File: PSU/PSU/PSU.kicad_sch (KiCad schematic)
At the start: 22 parts, among them J1 12V AC, J2 Switch, J3 Conn_02x08_Odd_Even, J4 Conn_02x08_Odd_Even, U1 LM7812, U2 LM7912, U3 LM7805_TO220

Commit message: .
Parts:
- removed J4: Conn_02x08_Odd_Even, symbol Connector_Generic:Conn_02x08_Odd_Even
- added J4: Power out, symbol Connector:Screw_Terminal_01x04
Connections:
- net +12V: now also J4.3 (Pin_3)
- net +5V: now also J4.4 (Pin_4)
- net -12V: now also J4.1 (Pin_1)
- net GNDREF: now also J4.2 (Pin_2)
- net CV: no longer names the net of J3.13 (Pin_13)
- net CV: no longer J3.14 (Pin_14)
- net GATE: no longer names the net of J3.15 (Pin_15)
- net GATE: no longer J3.16 (Pin_16)
- no-connect marks 0 -> 4
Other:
- moved on the sheet: C10

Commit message: .
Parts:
- added C11: 1uF, symbol Device:C_Small
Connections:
- net +12V: now also C11.1
- net GNDREF: now also C11.2
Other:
- moved on the sheet: C10, C7, C8, C9, D3, U1, U2

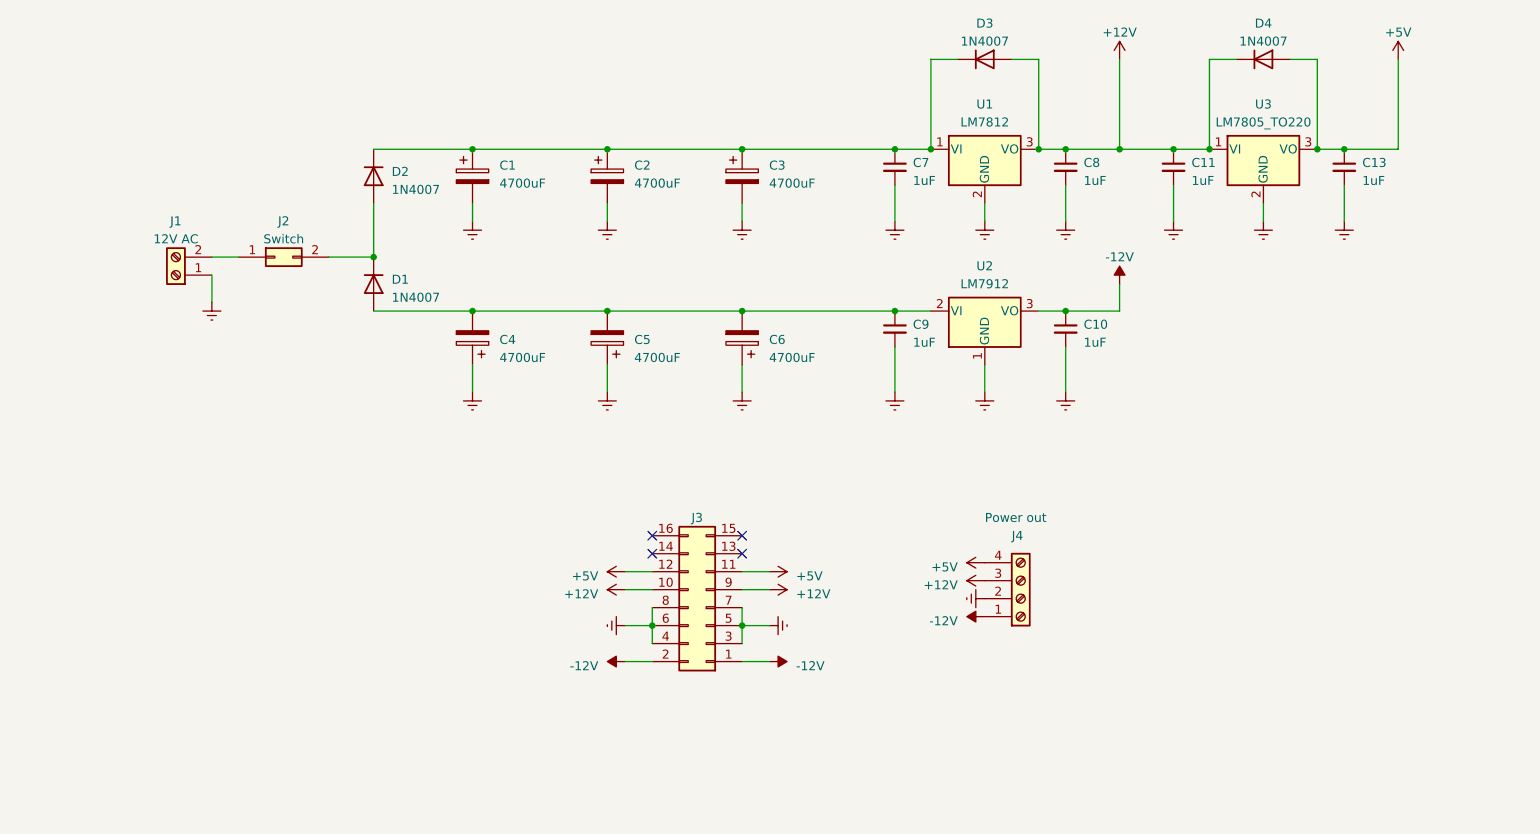
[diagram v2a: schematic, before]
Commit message: Option for center tapped transformer
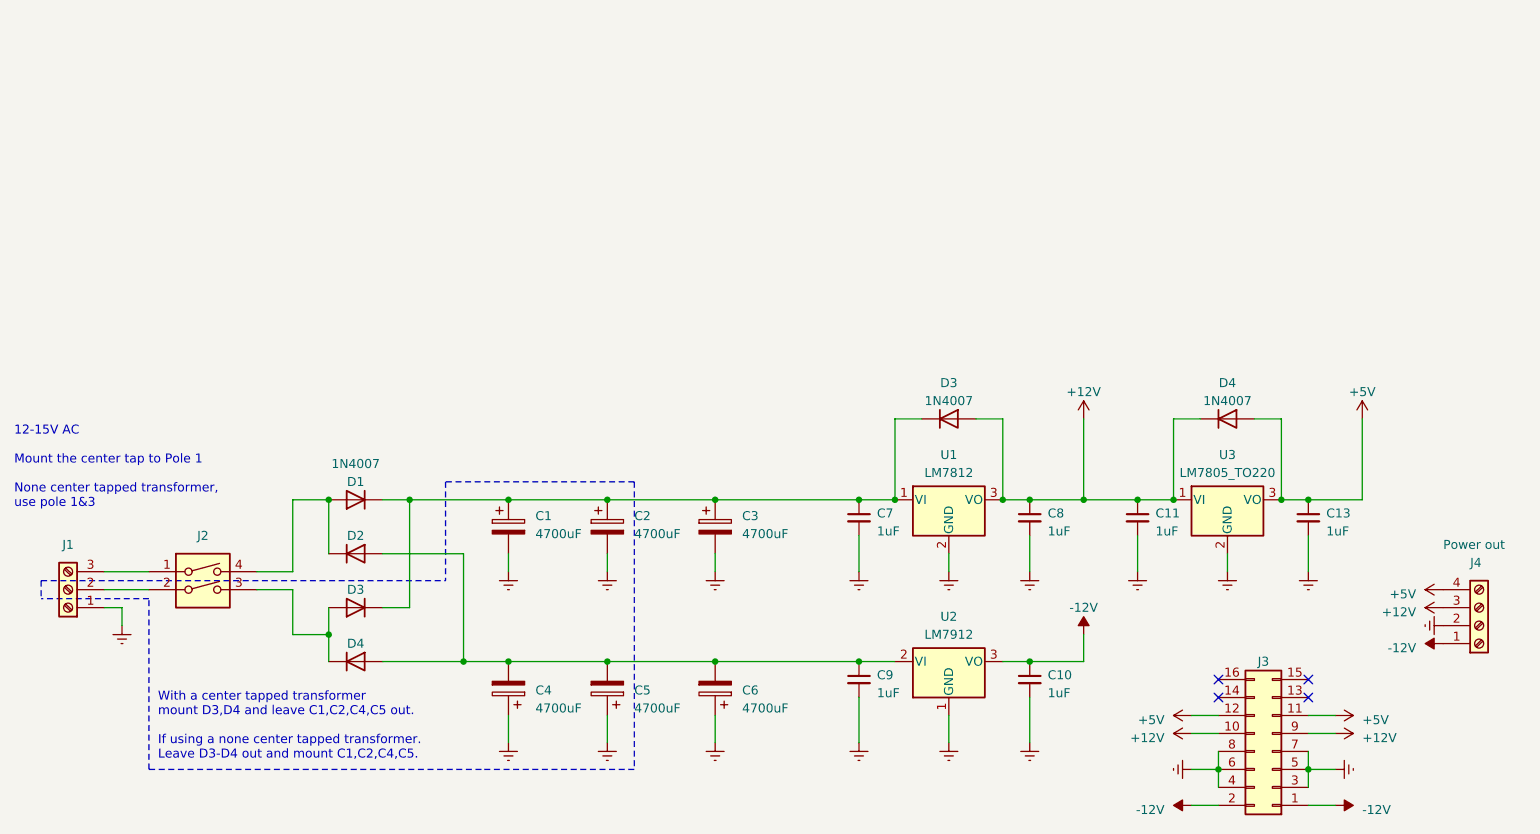
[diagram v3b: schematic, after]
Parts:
- removed J1: 12V AC, symbol Connector:Screw_Terminal_01x02
- removed J2: Switch, symbol Connector_Generic:Conn_02x01
- added D2, D4: 1N4007, Diode_THT:D_DO-41_SOD81_P10.16mm_Horizontal, symbol Diode:1N4007
- added J1: Screw_Terminal_01x03, symbol Connector:Screw_Terminal_01x03
- added J2: SW_DIP_x02, symbol Switch:SW_DIP_x02
- C1, C2, C3, C4, C5, C6: footprint (none) -> Capacitor_THT:CP_Radial_D18.0mm_P7.50mm
- renumbered D2 to D1, D1 to D3
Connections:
- net GNDREF: now also J1.1 (Pin_1)
- net at C4.2, C5.2, C6.2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: now also D2.2 (A), D4.2 (A); no longer D3.2 (A)
- net at D3.1 (K): now also C1.1, C2.1, C3.1, C7.1, D1.1 (K), D3.1 (K), U1.1 (VI); no longer D1.2 (A)
- new net: D3.2 (A), D4.1 (K), J2.3
- new net: D1.2 (A), D2.1 (K), J2.4
- new net: J1.3 (Pin_3), J2.1
- new net: J1.2 (Pin_2), J2.2
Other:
- note added: "12-15V AC Mount the center tap to Pole 1 None center tapped transformer, use pole 1&3"
- note added: "With a center tapped transformer mount D3,D4 and leave C1,C2,C4,C5 out. If using a none center tapped transformer. Leave D3-D4 out and mount C1,C2,C4,C5."
- moved on the sheet: C1, C10, C11, C13, C2, C3, C4, C5, C6, C7, C8, C9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

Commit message: PCD Fixed
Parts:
- C10, C11, C13, C7, C8, C9: footprint (none) -> Capacitor_THT:C_Rect_L7.0mm_W3.5mm_P5.00mm
- J1: footprint (none) -> Connector_JST:JST_NV_B03P-NV_1x03_P5.00mm_Vertical
- J2: footprint (none) -> Connector_PinSocket_2.54mm:PinSocket_2x02_P2.54mm_Vertical
- J3: footprint (none) -> Connector_IDC:IDC-Header_2x08_P2.54mm_Vertical
- J4: footprint (none) -> Connector_JST:JST_NV_B04P-NV_1x04_P5.00mm_Vertical
- renumbered D3 to D5, D4 to D6
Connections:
- net GNDREF: now also J1.3 (Pin_3); no longer J1.1 (Pin_1)
- net at D3.2 (A), D4.1 (K): now also J2.4; no longer J2.3
- net at D1.2 (A), D2.1 (K): now also J2.3; no longer J2.4
- net at J2.1: now also J1.1 (Pin_1); no longer J1.3 (Pin_3)
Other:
- moved on the sheet: J1
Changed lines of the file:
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@@
-    (stroke (width 0) (type default))
-  )
-  (wire (pts (xy 49.53 121.92) (xy 55.88 121.92))
     (stroke (width 0) (type default))
   )
@@
     (stroke (width 0) (type dash_dot) (color 255 176 22 1))
   )
+  (wire (pts (xy 41.91 119.38) (xy 55.88 119.38))
+    (stroke (width 0) (type default))
+  )
   (wire (pts (xy 195.58 109.22) (xy 200.66 109.22))
     (stroke (width 0) (type default))
@@
     (stroke (width 0) (type default))
   )
+  (wire (pts (xy 41.91 124.46) (xy 52.07 124.46))
+    (stroke (width 0) (type default))
+  )
   (wire (pts (xy 120.65 139.7) (xy 120.65 143.51))
-    (stroke (width 0) (type default))
-  )
-  (wire (pts (xy 49.53 124.46) (xy 52.07 124.46))
     (stroke (width 0) (type default))
   )
@@
     (stroke (width 0) (type default))
   )
-  (wire (pts (xy 49.53 119.38) (xy 55.88 119.38))
-    (stroke (width 0) (type default))
-  )
   (polyline (pts (xy 55.88 123.19) (xy 40.64 123.19))
     (stroke (width 0) (type dash_dot) (color 255 176 22 1))
@@
   )
   (wire (pts (xy 187.96 109.22) (xy 195.58 109.22))
+    (stroke (width 0) (type default))
+  )
+  (wire (pts (xy 41.91 121.92) (xy 55.88 121.92))
     (stroke (width 0) (type default))
   )
@@
       (effects (font (size 1.27 1.27)) (justify left))
     )
-    (property "Footprint" "" (at 156.21 134.62 0)
+    (property "Footprint" "Capacitor_THT:C_Rect_L7.0mm_W3.5mm_P5.00mm" (at 156.21 134.62 0)
       (effects (font (size 1.27 1.27)) hide)
     )
@@
       (effects (font (size 1.27 1.27)) hide)
     )
-    (property "Footprint" "" (at 214.63 144.78 0)
+    (property "Footprint" "Connector_IDC:IDC-Header_2x08_P2.54mm_Vertical" (at 214.63 144.78 0)
       (effects (font (size 1.27 1.27)) hide)
     )
@@
       (effects (font (size 1.27 1.27)) (justify left))
     )
-    (property "Footprint" "" (at 180.34 111.76 0)
+    (property "Footprint" "Capacitor_THT:C_Rect_L7.0mm_W3.5mm_P5.00mm" (at 180.34 111.76 0)
       (effects (font (size 1.27 1.27)) hide)
     )
@@
       (effects (font (size 1.27 1.27)) (justify left))
     )
-    (property "Footprint" "" (at 195.58 111.76 0)
+    (property "Footprint" "Capacitor_THT:C_Rect_L7.0mm_W3.5mm_P5.00mm" (at 195.58 111.76 0)
       (effects (font (size 1.27 1.27)) hide)
     )
@@
       (effects (font (size 1.27 1.27)) (justify left))
     )
-    (property "Footprint" "" (at 243.84 127 0)
+    (property "Footprint" "Connector_JST:JST_NV_B04P-NV_1x04_P5.00mm_Vertical" (at 243.84 127 0)
       (effects (font (size 1.27 1.27)) hide)
     )
@@
       (effects (font (size 1.27 1.27)) (justify left))
     )
-    (property "Footprint" "" (at 219.71 111.76 0)
+    (property "Footprint" "Capacitor_THT:C_Rect_L7.0mm_W3.5mm_P5.00mm" (at 219.71 111.76 0)
       (effects (font (size 1.27 1.27)) hide)
     )
@@
   (symbol (lib_id "Diode:1N4007") (at 208.28 97.79 0) (unit 1)
     (in_bom yes) (on_board yes) (dnp no) (fields_autoplaced)
-    (property "Reference" "D4" (at 208.28 92.71 0)
+    (property "Reference" "D6" (at 208.28 92.71 0)
       (effects (font (size 1.27 1.27)))
     )
@@
       (project "PSU"
         (path "/780e3006-e51c-4736-8f8a-c1e1cf3a82ba"
-          (reference "D4") (unit 1)
+          (reference "D6") (unit 1)
         )
       )
@@
       (effects (font (size 1.27 1.27)) hide)
     )
-    (property "Footprint" "" (at 63.5 121.92 0)
+    (property "Footprint" "Connector_PinSocket_2.54mm:PinSocket_2x02_P2.54mm_Vertical" (at 63.5 125.73 0)
       (effects (font (size 1.27 1.27)) hide)
     )
@@
     )
   )
-  (symbol (lib_id "Connector:Screw_Terminal_01x03") (at 44.45 121.92 180) (unit 1)
+  (symbol (lib_id "Connector:Screw_Terminal_01x03") (at 46.99 121.92 0) (unit 1)
     (in_bom yes) (on_board yes) (dnp no)
-    (property "Reference" "J1" (at 44.45 115.57 0)
-      (effects (font (size 1.27 1.27)))
-    )
-    (property "Value" "Screw_Terminal_01x03" (at 44.45 116.84 0)
-      (effects (font (size 1.27 1.27)) hide)
-    )
-    (property "Footprint" "" (at 44.45 121.92 0)
-      (effects (font (size 1.27 1.27)) hide)
-    )
-    (property "Datasheet" "~" (at 44.45 121.92 0)
+    (property "Reference" "J1" (at 46.99 128.27 0)
+      (effects (font (size 1.27 1.27)))
+    )
+    (property "Value" "Screw_Terminal_01x03" (at 46.99 127 0)
+      (effects (font (size 1.27 1.27)) hide)
+    )
+    (property "Footprint" "Connector_JST:JST_NV_B03P-NV_1x03_P5.00mm_Vertical" (at 46.99 121.92 0)
+      (effects (font (size 1.27 1.27)) hide)
+    )
+    (property "Datasheet" "~" (at 46.99 121.92 0)
       (effects (font (size 1.27 1.27)) hide)
     )
@@
   (symbol (lib_id "Diode:1N4007") (at 168.91 97.79 0) (unit 1)
     (in_bom yes) (on_board yes) (dnp no) (fields_autoplaced)
-    (property "Reference" "D3" (at 168.91 92.71 0)
+    (property "Reference" "D5" (at 168.91 92.71 0)
       (effects (font (size 1.27 1.27)))
     )
@@
       (project "PSU"
         (path "/780e3006-e51c-4736-8f8a-c1e1cf3a82ba"
-          (reference "D3") (unit 1)
+          (reference "D5") (unit 1)
         )
       )
@@
       (effects (font (size 1.27 1.27)) (justify left))
     )
-    (property "Footprint" "" (at 180.34 134.62 0)
+    (property "Footprint" "Capacitor_THT:C_Rect_L7.0mm_W3.5mm_P5.00mm" (at 180.34 134.62 0)
       (effects (font (size 1.27 1.27)) hide)
     )
@@
       (effects (font (size 1.27 1.27)) (justify left))
     )
-    (property "Footprint" "" (at 156.21 111.76 0)
-      (effects (font (size 1.27 1.27)) hide)
-    )
+    (property "Footprint" "Capacitor_THT:C_Rect_L7.0mm_W3.5mm_P5.00mm" (at 156.21 111.76 0)
+      (effects (font (size 1.27 1.27)) hide)
+    )
